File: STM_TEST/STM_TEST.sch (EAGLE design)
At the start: 53 parts, among them U1 TPS2115APWR, U2 AZ1117EH-3.3TRG1, Y1 ECS-80-S-4X, Y2 ECS-80-S-4X

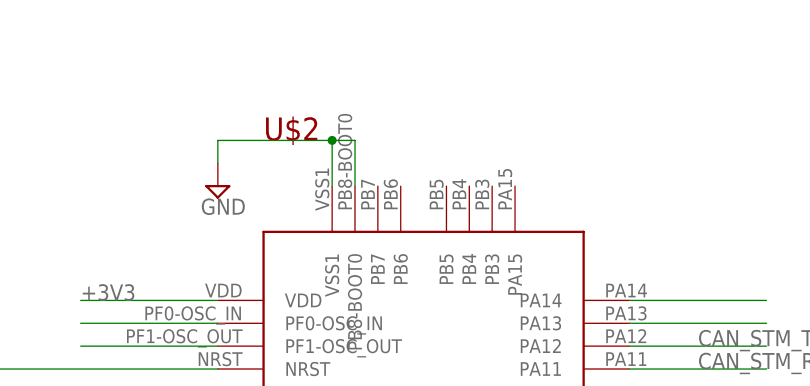
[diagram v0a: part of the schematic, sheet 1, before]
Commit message: Routed USART
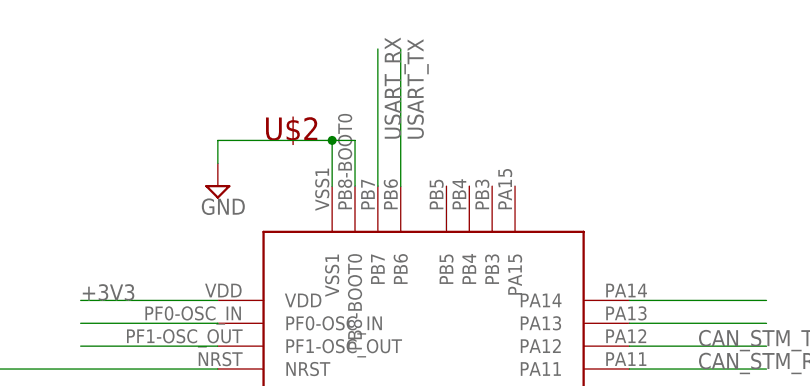
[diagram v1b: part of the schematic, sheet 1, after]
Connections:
- removed net UART_RXD: PCB1.GPIO15
- removed net UART_TXD: PCB1.GPIO14
- new net USART_RX: PCB1.GPIO14, U$2.PB7
- new net USART_TX: PCB1.GPIO15, U$2.PB6
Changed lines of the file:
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@@
+</segment>
+</net>
+<net name="USART_RX" class="0">
+<segment>
+<pinref part="U$2" gate="G$1" pin="PB7"/>
+<wire x1="281.94" y1="231.14" x2="281.94" y2="246.38" width="0.1524" layer="91"/>
+<label x="284.48" y="236.22" size="1.778" layer="95" rot="R90"/>
+</segment>
+</net>
+<net name="USART_TX" class="0">
+<segment>
+<pinref part="U$2" gate="G$1" pin="PB6"/>
+<wire x1="284.48" y1="231.14" x2="284.48" y2="246.38" width="0.1524" layer="91"/>
+<label x="287.02" y="236.22" size="1.778" layer="95" rot="R90"/>
 </segment>
 </net>
@@
 </segment>
 </net>
-<net name="UART_RXD" class="0">
+<net name="USART_TX" class="0">
 <segment>
 <pinref part="PCB1" gate="G$1" pin="GPIO15"/>
@@
 </segment>
 </net>
-<net name="UART_TXD" class="0">
+<net name="USART_RX" class="0">
 <segment>
 <pinref part="PCB1" gate="G$1" pin="GPIO14"/>

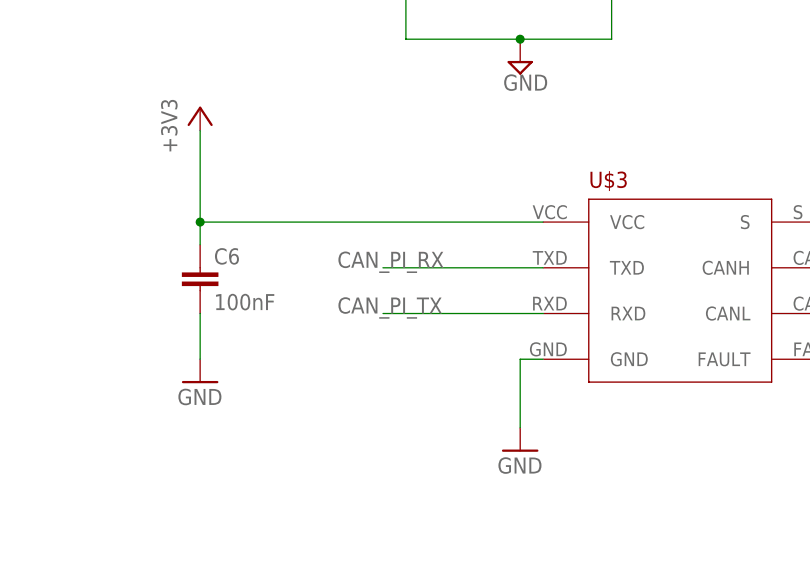
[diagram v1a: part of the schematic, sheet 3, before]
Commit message: Routing Complete
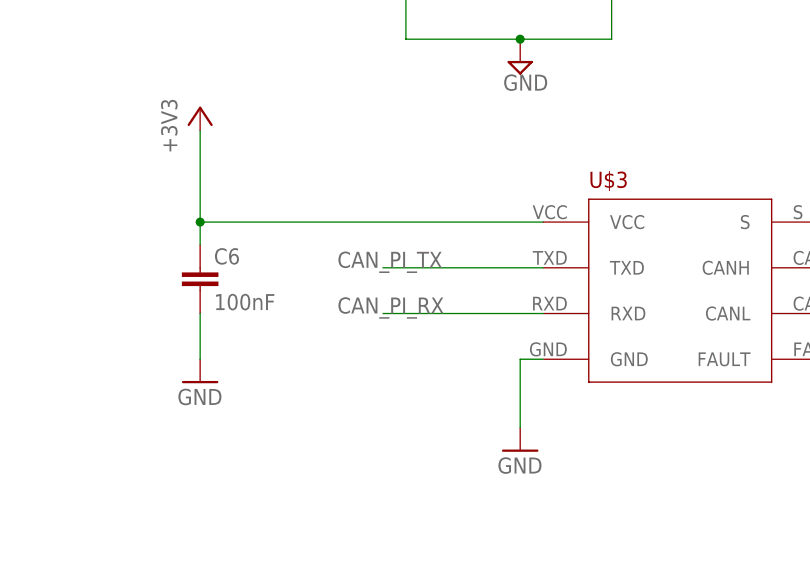
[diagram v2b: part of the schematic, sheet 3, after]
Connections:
- net CAN_PI_RX: now also U$3.RXD; no longer U$3.TXD
- net CAN_PI_TX: now also U$3.TXD; no longer U$3.RXD
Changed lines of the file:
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@@
 <net name="CAN_PI_RX" class="0">
+<segment>
+<pinref part="U$5" gate="G$1" pin="RXCAN"/>
+<wire x1="299.72" y1="210.82" x2="279.4" y2="210.82" width="0.1524" layer="91"/>
+<label x="276.86" y="210.82" size="1.778" layer="95"/>
+</segment>
+<segment>
+<pinref part="U$3" gate="G$1" pin="RXD"/>
+<wire x1="236.22" y1="157.48" x2="218.44" y2="157.48" width="0.1524" layer="91"/>
+<label x="213.36" y="157.48" size="1.778" layer="95"/>
+</segment>
+</net>
+<net name="CAN_PI_TX" class="0">
+<segment>
+<pinref part="U$5" gate="G$1" pin="TXCAN"/>
+<wire x1="299.72" y1="213.36" x2="279.4" y2="213.36" width="0.1524" layer="91"/>
+<label x="276.86" y="213.36" size="1.778" layer="95"/>
+</segment>
 <segment>
 <pinref part="U$3" gate="G$1" pin="TXD"/>
@@
 <label x="213.36" y="162.56" size="1.778" layer="95"/>
 </segment>
-<segment>
-<pinref part="U$5" gate="G$1" pin="RXCAN"/>
-<wire x1="299.72" y1="210.82" x2="279.4" y2="210.82" width="0.1524" layer="91"/>
-<label x="276.86" y="210.82" size="1.778" layer="95"/>
-</segment>
 </net>
-<net name="CAN_PI_TX" class="0">
-<segment>
-<pinref part="U$3" gate="G$1" pin="RXD"/>
-<wire x1="236.22" y1="157.48" x2="218.44" y2="157.48" width="0.1524" layer="91"/>
-<label x="213.36" y="157.48" size="1.778" layer="95"/>
-</segment>
-<segment>
-<pinref part="U$5" gate="G$1" pin="TXCAN"/>
-<wire x1="299.72" y1="213.36" x2="279.4" y2="213.36" width="0.1524" layer="91"/>
-<label x="276.86" y="213.36" size="1.778" layer="95"/>
-</segment>
-</net>

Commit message: finished
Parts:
- added D2: (no value), SparkFun-LED:LED0603
- added R15: 10k, SparkFun-Resistors:100KOHM-0603-1/10W-1%
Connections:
- new net N$4: D2.A, R15.1
- new net N$5: R15.2, U$2.PB4
- net GND: now also D2.C
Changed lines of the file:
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@@
 <part name="C21" library="SparkFun-Capacitors" deviceset="1.0UF" device="-0603-16V-10%" value="1.0uF"/>
 <part name="GND34" library="supply1" library_urn="urn:adsk.eagle:library:371" deviceset="GND" device=""/>
+<part name="R15" library="SparkFun-Resistors" library_urn="urn:adsk.eagle:library:532" deviceset="100KOHM" device="-0603-1/10W-1%" package3d_urn="urn:adsk.eagle:package:39650/1" value="10k"/>
+<part name="GND35" library="supply1" library_urn="urn:adsk.eagle:library:371" deviceset="GND" device=""/>
+<part name="D2" library="SparkFun-LED" deviceset="LED" device="0603"/>
 </parts>
 <sheets>
@@
 <instance part="+3V7" gate="G$1" x="251.46" y="78.74">
 <attribute name="VALUE" x="248.92" y="73.66" size="1.778" layer="96" rot="R90"/>
+</instance>
+<instance part="R15" gate="G$1" x="320.04" y="248.92" rot="R180">
+<attribute name="NAME" x="320.04" y="247.396" size="1.778" layer="95" font="vector" rot="R180" align="bottom-center"/>
+<attribute name="VALUE" x="320.04" y="250.444" size="1.778" layer="96" font="vector" rot="R180" align="top-center"/>
+</instance>
+<instance part="GND35" gate="1" x="330.2" y="228.6">
+<attribute name="VALUE" x="327.66" y="226.06" size="1.778" layer="96"/>
+</instance>
+<instance part="D2" gate="D1" x="330.2" y="241.3">
+<attribute name="NAME" x="326.771" y="236.728" size="1.778" layer="95" font="vector" rot="R90"/>
+<attribute name="VALUE" x="332.105" y="236.728" size="1.778" layer="96" font="vector" rot="R90" align="top-left"/>
 </instance>
 </instances>
@@
 <junction x="251.46" y="45.72"/>
 </segment>
+<segment>
+<pinref part="GND35" gate="1" pin="GND"/>
+<pinref part="D2" gate="D1" pin="C"/>
+<wire x1="330.2" y1="231.14" x2="330.2" y2="236.22" width="0.1524" layer="91"/>
+</segment>
 </net>
 <net name="+3V3" class="0">
@@
 </segment>
 </net>
+<net name="N$4" class="0">
+<segment>
+<pinref part="R15" gate="G$1" pin="1"/>
+<wire x1="325.12" y1="248.92" x2="330.2" y2="248.92" width="0.1524" layer="91"/>
+<pinref part="D2" gate="D1" pin="A"/>
+<wire x1="330.2" y1="243.84" x2="330.2" y2="248.92" width="0.1524" layer="91"/>
+</segment>
+</net>
+<net name="N$5" class="0">
+<segment>
+<pinref part="U$2" gate="G$1" pin="PB4"/>
+<pinref part="R15" gate="G$1" pin="2"/>
+<wire x1="292.1" y1="231.14" x2="292.1" y2="248.92" width="0.1524" layer="91"/>
+<wire x1="292.1" y1="248.92" x2="314.96" y2="248.92" width="0.1524" layer="91"/>
+</segment>
+</net>
